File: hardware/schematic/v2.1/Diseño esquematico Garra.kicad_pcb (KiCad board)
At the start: 2 copper layers, 85.5 x 137 mm, 26 parts

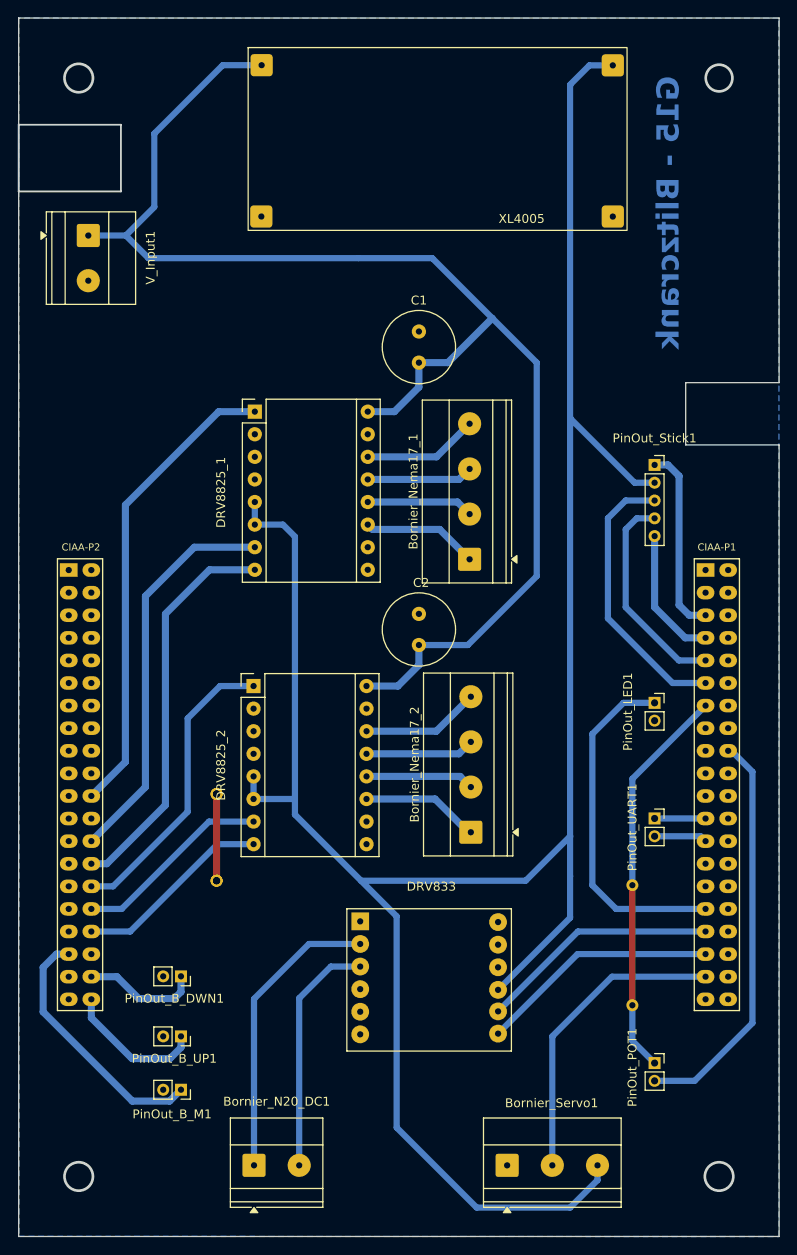
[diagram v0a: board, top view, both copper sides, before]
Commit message: Pcb branch (#11)
* refactor

* feat: PCB routing first stage completed

* docs: Schematics PDF added

* fix: PCB border colision

* feat: Copper layers added to the PCB

* feat: New PCB design with new components [LED, B_M]

* feat: add through holes for connectivity & GNDs links

* feat: hole diameter adjustment

* fix: PDF

* feat: change route system in PCB

* feat: add new esp32 schematic

* feat: complete PCB

* feat: take png and pdf from finished schematic

* feat: valid pdf PCB template

* fix: Expand PCB routes and copper holes

---------

Co-authored-by: ManuSavenia <saveniamanuel@egmail.com>
Co-authored-by: Iván Valentín Polanis <polanis.ivan@alu.ing.unlp.edu.ar>
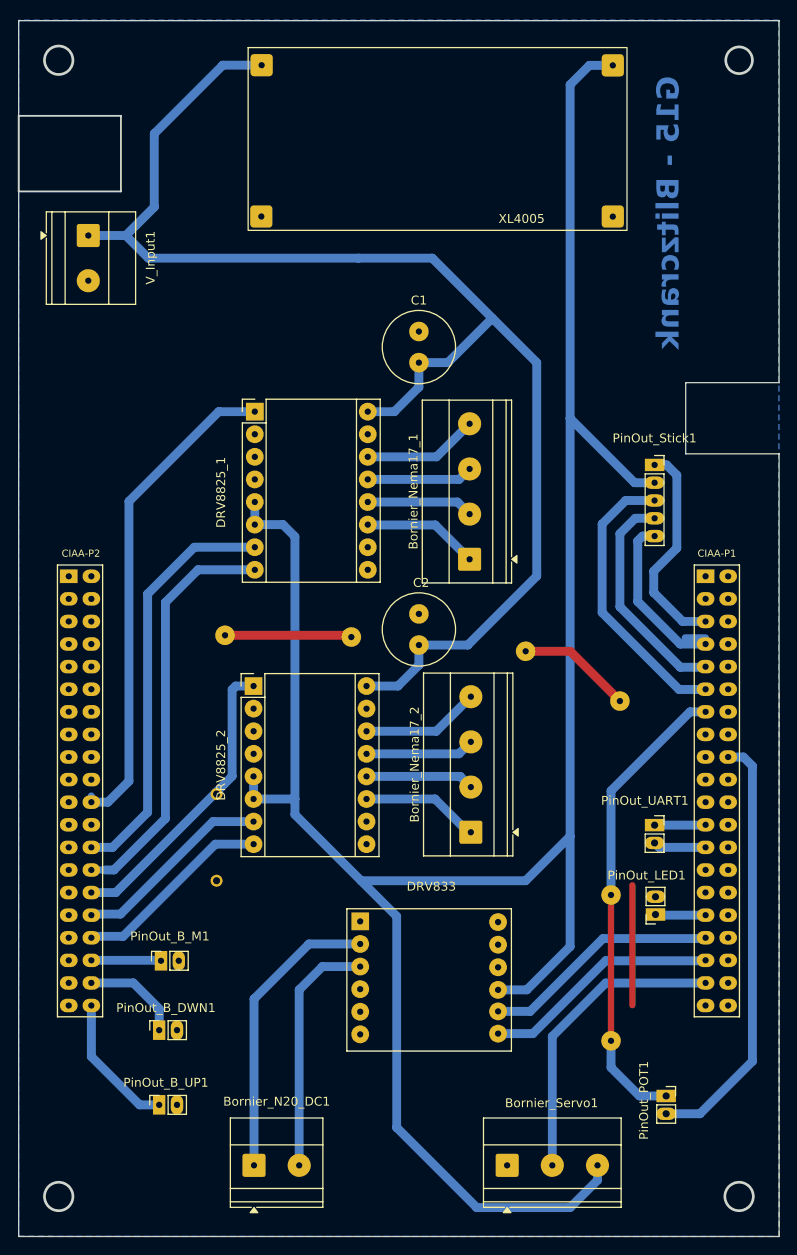
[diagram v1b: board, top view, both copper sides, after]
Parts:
- removed the ? at (57.2, 122.0)
- removed the ? at (57.2, 112.2)
- added ?: , , F.Cu at (72.4, 94.6)
- added ?: , , F.Cu at (92.0, 96.2)
- added ?: , , F.Cu at (102.6, 101.8)
- added ?: , , F.Cu at (58.2, 94.4)
- moved PinOut_LED1 23.8 mm to (106.6, 125.8), turned to 180 degrees
- moved PinOut_B_M1 14.7 mm to (51.0, 131.0), turned to 90 degrees
- moved PinOut_B_UP1 8.08 mm to (50.8, 147.2), turned to 90 degrees
- moved PinOut_B_DWN1 6.53 mm to (50.8, 138.8), turned to 90 degrees
- moved ? 4.66 mm to (101.6, 140.0)
- moved PinOut_POT1 3.92 mm to (107.8, 146.2)
- moved ? 2.64 mm to (101.6, 123.6)
- moved PinOut_UART1 0.75 mm to (106.5, 115.8)
- moved CIAA-P1 0.70 mm to (113.5, 111.9)
- moved CIAA-P2 0.70 mm to (41.9, 111.9)
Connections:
- CIAA-P2 pad 35: B_M -> unconnected-(CIAA-P2-GPIO6-Pad35)
- CIAA-P2 pad 36: unconnected-(CIAA-P2-GPIO5-Pad36) -> B_M
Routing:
- net LED: track 39.3 -> 5.84 mm
- net B_M: track 28.7 -> 8.13 mm
- net GND: track 9.75 -> 27.2 mm
- net VRX: track 30.8 -> 46.1 mm
- net POT: track 44.6 -> 54.5 mm
- net GND_Stick: track 15.2 -> 19.5 mm
- net Stick_ON: track 21.2 -> 24.4 mm
- net GND_POT: track 45.6 -> 48.5 mm
- net VRY: track 24.0 -> 26.7 mm
- net EN1: track 53.2 -> 55.7 mm
- net STEP1: track 44.6 -> 46.7 mm
- net DIR1: track 44.7 -> 46.6 mm
- net 5V: track 263.6 -> 265.5 mm
- net B_DWN: track 13.2 -> 11.7 mm
- net MOTOR_GND: track 27.1 -> 27.7 mm
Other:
- board size 85.5 x 137 mm -> 85.5 x 136.7 mm

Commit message: feat: Change PCB design and clearance
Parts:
- removed the ? at (102.6, 101.8)
- PinOut_B_DWN1, PinOut_B_M1, PinOut_B_UP1, PinOut_LED1, PinOut_POT1: footprint Connector_PinSocket_2.00mm:PinSocket_1x02_P2.00mm_Vertical -> LIBRERIA_EDU_CIAA_NXP:PinSocket_1x02_P2.54mm_Vertical
- moved PinOut_Stick1 17.6 mm to (106.5, 92.9)
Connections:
- PinOut_Stick1 pad 2: 5V -> GND_Stick
- PinOut_Stick1 pad 3: VRX -> VRY
- PinOut_Stick1 pad 4: VRY -> VRX
- PinOut_Stick1 pad 5: GND_Stick -> 5V
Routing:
- net VRX: track 46.1 -> 5.78 mm
- net VRY: track 26.7 -> 6.34 mm
- net Stick_ON: track 24.4 -> 5.74 mm
- net GND_Stick: track 19.5 -> 5.74 mm
- net GND: track 27.2 -> 14.3 mm
- net 5V: track 265.5 -> 263.0 mm
- net POT: track 54.5 -> 52.7 mm
